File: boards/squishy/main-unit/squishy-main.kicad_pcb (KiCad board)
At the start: 6 copper layers, 0 parts

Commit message: squishy: main: updated the board stackup and went from 6 to 8 layers
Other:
- copper layers 6 -> 8

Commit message: squishy: main: handful of misc updates all jumbled together
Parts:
- added C1: 10n, Capacitor_SMD:C_0603_1608Metric, F.Cu at (203.4, 112.9)
- added C10: 100n, Capacitor_SMD:C_0402_1005Metric, F.Cu at (265.3, 88.3)
- added C11: 100n, Capacitor_SMD:C_0603_1608Metric, F.Cu at (253.8, 91.6)
- added C12: 4u7, Capacitor_SMD:C_0603_1608Metric, F.Cu at (253.8, 94.1)
- added C13: 100n, Capacitor_SMD:C_0603_1608Metric, F.Cu at (253.8, 96.6)
- added C14: 100n, Capacitor_SMD:C_0603_1608Metric, F.Cu at (253.8, 99.2)
- added C15: 10n, Capacitor_SMD:C_0603_1608Metric, F.Cu at (257.8, 86.6)
- added C16: 10u, Capacitor_SMD:C_0603_1608Metric, F.Cu at (257.8, 89.1)
- added C17: 1u, Capacitor_SMD:C_0603_1608Metric, F.Cu at (257.8, 91.6)
- added C18: 10n, Capacitor_SMD:C_0603_1608Metric, F.Cu at (257.8, 94.1)
- added C19: 100n, Capacitor_SMD:C_0603_1608Metric, F.Cu at (203.4, 115.4)
- added C2: 100n, Capacitor_SMD:C_0402_1005Metric, F.Cu at (210.7, 36.6)
- added C20: 1u, Capacitor_SMD:C_0603_1608Metric, F.Cu at (203.4, 117.9)
- added C21: 1u, Capacitor_SMD:C_0603_1608Metric, F.Cu at (203.4, 120.4)
- added C22: 10n, Capacitor_SMD:C_0603_1608Metric, F.Cu at (203.4, 122.9)
- added C23: 100n, Capacitor_SMD:C_0603_1608Metric, F.Cu at (203.4, 21.8)
- added C24: 2u2, Capacitor_SMD:C_0603_1608Metric, F.Cu at (203.4, 24.3)
- added C25: 100n, Capacitor_SMD:C_0603_1608Metric, F.Cu at (203.4, 26.9)
- added C26: 12n, Capacitor_SMD:C_0402_1005Metric, F.Cu at (210.7, 44.5)
- added C27: 10u, Capacitor_SMD:C_0805_2012Metric, F.Cu at (244.6, 19.6)
- added C28: 2u2, Capacitor_SMD:C_1812_4532Metric, F.Cu at (255.3, 67.2)
- added C29: 10u, Capacitor_SMD:C_0805_2012Metric, F.Cu at (244.6, 22.6)
- added C3: 100n, Capacitor_SMD:C_0402_1005Metric, F.Cu at (210.7, 38.6)
- added C30: 1u, Capacitor_SMD:C_0603_1608Metric, F.Cu at (203.4, 29.4)
- added C31: 100n, Capacitor_SMD:C_0402_1005Metric, F.Cu at (210.7, 46.5)
- added C32: 10u, Capacitor_SMD:C_0805_2012Metric, F.Cu at (244.6, 25.6)
- added C33: 10u, Capacitor_SMD:C_0805_2012Metric, F.Cu at (244.6, 28.6)
- added C34: 100n, Capacitor_SMD:C_0402_1005Metric, F.Cu at (210.7, 48.4)
- added C35: 100n, Capacitor_SMD:C_0402_1005Metric, F.Cu at (213.6, 36.6)
- added C36: 100n, Capacitor_SMD:C_0402_1005Metric, F.Cu at (213.6, 38.6)
- added C37: 100n, Capacitor_SMD:C_0402_1005Metric, F.Cu at (213.6, 40.6)
- added C38: 820p, Capacitor_SMD:C_0402_1005Metric, F.Cu at (213.6, 42.5)
- added C39: 1u, Capacitor_SMD:C_0603_1608Metric, F.Cu at (203.4, 31.9)
- added C4: 100n, Capacitor_SMD:C_0402_1005Metric, F.Cu at (210.7, 40.6)
- added C40: 1u, Capacitor_SMD:C_0603_1608Metric, F.Cu at (203.4, 34.4)
- added C41: 100n, Capacitor_SMD:C_0402_1005Metric, F.Cu at (213.6, 44.5)
- added C42: 1u, Capacitor_SMD:C_0603_1608Metric, F.Cu at (207.4, 19.3)
- added C43: 1u, Capacitor_SMD:C_0603_1608Metric, F.Cu at (207.4, 21.8)
- added C44: 100n, Capacitor_SMD:C_0402_1005Metric, F.Cu at (213.6, 46.5)
- added C45: 1u, Capacitor_SMD:C_0603_1608Metric, F.Cu at (207.4, 24.3)
- added C46: 1u, Capacitor_SMD:C_0603_1608Metric, F.Cu at (207.4, 26.9)
- added C47: 1u, Capacitor_SMD:C_0603_1608Metric, F.Cu at (207.4, 29.4)
- added C48: 1u, Capacitor_SMD:C_0603_1608Metric, F.Cu at (207.4, 31.9)
- added C49: 300p, Capacitor_SMD:C_0603_1608Metric, F.Cu at (257.8, 96.6)
- added C5: 100n, Capacitor_SMD:C_0402_1005Metric, F.Cu at (210.7, 42.5)
- added C50: 100n, Capacitor_SMD:C_0402_1005Metric, F.Cu at (213.6, 48.4)
- added C51: 10n, Capacitor_SMD:C_0402_1005Metric, F.Cu at (216.5, 36.6)
- added C52: 100n, Capacitor_SMD:C_0402_1005Metric, F.Cu at (216.5, 38.6)
- added C53: 100n, Capacitor_SMD:C_0402_1005Metric, F.Cu at (216.5, 40.6)
- added C54: 100n, Capacitor_SMD:C_0402_1005Metric, F.Cu at (216.5, 42.5)
- added C55: 10n, Capacitor_SMD:C_0402_1005Metric, F.Cu at (216.5, 44.5)
- added C56: 1n, Capacitor_SMD:C_0402_1005Metric, F.Cu at (216.5, 46.5)
- added C57: 100n, Capacitor_SMD:C_0402_1005Metric, F.Cu at (216.5, 48.4)
- added C58: 10n, Capacitor_SMD:C_0402_1005Metric, F.Cu at (219.3, 36.6)
- added C59: 1n, Capacitor_SMD:C_0402_1005Metric, F.Cu at (219.3, 38.6)
- added C6: 1u, Capacitor_SMD:C_0603_1608Metric, F.Cu at (203.4, 19.3)
- added C60: 100n, Capacitor_SMD:C_0402_1005Metric, F.Cu at (219.3, 40.6)
- added C61: 10n, Capacitor_SMD:C_0402_1005Metric, F.Cu at (219.3, 42.5)
- added C62: 1n, Capacitor_SMD:C_0402_1005Metric, F.Cu at (219.3, 44.5)
- added C63: 1u, Capacitor_SMD:C_0402_1005Metric, F.Cu at (219.3, 46.5)
- added C64: 4u7, Capacitor_SMD:C_0603_1608Metric, F.Cu at (207.4, 34.4)
- added C65: 100n, Capacitor_SMD:C_0402_1005Metric, F.Cu at (219.3, 48.4)
- added C66: 100n, Capacitor_SMD:C_0402_1005Metric, F.Cu at (222.2, 36.6)
- added C67: 10n, Capacitor_SMD:C_0402_1005Metric, F.Cu at (222.2, 38.6)
- added C68: 10n, Capacitor_SMD:C_0402_1005Metric, F.Cu at (222.2, 40.6)
- added C69: 10n, Capacitor_SMD:C_0402_1005Metric, F.Cu at (222.2, 42.5)
- added C7: 1n, Capacitor_SMD:C_0603_1608Metric, F.Cu at (253.8, 86.6)
- added C70: 10n, Capacitor_SMD:C_0402_1005Metric, F.Cu at (222.2, 44.5)
- added C71: 4u7, Capacitor_SMD:C_0603_1608Metric, F.Cu at (211.4, 19.3)
- added C72: 100n, Capacitor_SMD:C_0402_1005Metric, F.Cu at (222.2, 46.5)
- added C73: 100n, Capacitor_SMD:C_0402_1005Metric, F.Cu at (222.2, 48.4)
- added C74: 100n, Capacitor_SMD:C_0402_1005Metric, F.Cu at (225.1, 36.6)
- added C75: 1u, Capacitor_SMD:C_0402_1005Metric, F.Cu at (225.1, 38.6)
- added C76: 1u, Capacitor_SMD:C_0402_1005Metric, F.Cu at (225.1, 40.6)
- added C77: 1u, Capacitor_SMD:C_0402_1005Metric, F.Cu at (225.1, 42.5)
- added C78: 1u, Capacitor_SMD:C_0402_1005Metric, F.Cu at (225.1, 44.5)
- added C79: 100n, Capacitor_SMD:C_0402_1005Metric, F.Cu at (225.1, 46.5)
- added C8: 100n, Capacitor_SMD:C_0603_1608Metric, F.Cu at (253.8, 89.1)
- added C80: 1u, Capacitor_SMD:C_0603_1608Metric, F.Cu at (203.4, 125.4)
- added C81: 100n, Capacitor_SMD:C_0402_1005Metric, F.Cu at (265.3, 90.3)
- added C82: 10n, Capacitor_SMD:C_0402_1005Metric, F.Cu at (265.3, 92.2)
- added C83: 100n, Capacitor_SMD:C_0402_1005Metric, F.Cu at (265.3, 94.2)
- added C84: 10n, Capacitor_SMD:C_0402_1005Metric, F.Cu at (265.3, 96.2)
- added C85: 1n, Capacitor_SMD:C_0402_1005Metric, F.Cu at (265.3, 98.2)
- added C86: 100n, Capacitor_SMD:C_0402_1005Metric, F.Cu at (225.1, 48.4)
- added C87: 1u, Capacitor_SMD:C_0603_1608Metric, F.Cu at (211.4, 21.8)
- added C88: 1u, Capacitor_SMD:C_0603_1608Metric, F.Cu at (211.4, 24.3)
- added C89: 10u, Capacitor_SMD:C_0603_1608Metric, F.Cu at (211.4, 26.9)
- added C9: 100n, Capacitor_SMD:C_0402_1005Metric, F.Cu at (265.3, 86.3)
- added C90: 22p, Capacitor_SMD:C_0603_1608Metric, F.Cu at (211.4, 29.4)
- added C91: 300p, Capacitor_SMD:C_0603_1608Metric, F.Cu at (257.8, 99.2)
- added C92: 100n, Capacitor_SMD:C_0603_1608Metric, F.Cu at (261.9, 86.6)
- added C93: 10u, Capacitor_SMD:C_0805_2012Metric, F.Cu at (276.1, 95.0)
- added C94: 47u, Capacitor_SMD:C_0805_2012Metric, F.Cu at (244.6, 31.6)
- added C95: 100n, Capacitor_SMD:C_0603_1608Metric, F.Cu at (211.4, 31.9)
- added D1: SS10P6-M3/86A, lethalbit-so:TO-277A-2, F.Cu at (256.1, 22.2)
- added D10: GREEN, LED_SMD:LED_0603_1608Metric_Pad1.05x0.95mm_HandSolder, F.Cu at (255.5, 57.0)
- added D11: GREEN, LED_SMD:LED_0603_1608Metric_Pad1.05x0.95mm_HandSolder, F.Cu at (255.5, 59.6)
- added D12: GREEN, LED_SMD:LED_0603_1608Metric_Pad1.05x0.95mm_HandSolder, F.Cu at (255.5, 62.2)
- added D13: 24.25V @ 120mA, Diode_SMD:D_SOD-323, F.Cu at (238.6, 63.9)
- added D14: TN1205H, Package_TO_SOT_SMD:TO-263-2, F.Cu at (237.2, 41.8)
- added D2: BLUE, LED_SMD:LED_0603_1608Metric_Pad1.05x0.95mm_HandSolder, F.Cu at (219.6, 112.9)
- added D3: PINK, LED_SMD:LED_0603_1608Metric_Pad1.05x0.95mm_HandSolder, F.Cu at (219.6, 115.5)
- added D4: WHITE, LED_SMD:LED_0603_1608Metric_Pad1.05x0.95mm_HandSolder, F.Cu at (219.6, 118.1)
- added D5: PINK, LED_SMD:LED_0603_1608Metric_Pad1.05x0.95mm_HandSolder, F.Cu at (219.6, 120.7)
- added D6: BLUE, LED_SMD:LED_0603_1608Metric_Pad1.05x0.95mm_HandSolder, F.Cu at (219.6, 123.3)
- added D7: WHITE, LED_SMD:LED_0603_1608Metric_Pad1.05x0.95mm_HandSolder, F.Cu at (255.5, 49.3)
- added D8: GREEN, LED_SMD:LED_0603_1608Metric_Pad1.05x0.95mm_HandSolder, F.Cu at (255.5, 51.9)
- added D9: GREEN, LED_SMD:LED_0603_1608Metric_Pad1.05x0.95mm_HandSolder, F.Cu at (255.5, 54.5)
- added F1: 7A, Fuse:Fuse_1206_3216Metric, F.Cu at (233.6, 64.1)
- added F2: 7A, Fuse:Fuse_1206_3216Metric, F.Cu at (275.7, 87.0)
- added FB1: 600 @ 100MHz, Resistor_SMD:R_0805_2012Metric, F.Cu at (220.1, 58.7)
- added FB2: 600 @ 100MHz, Resistor_SMD:R_0805_2012Metric, F.Cu at (220.1, 61.7)
- added FID1: Fiducial, Fiducial:Fiducial_0.75mm_Mask1.5mm, F.Cu at (245.8, 37.2)
- added FID2: Fiducial, Fiducial:Fiducial_0.75mm_Mask1.5mm, F.Cu at (245.8, 40.2)
- added FID3: Fiducial, Fiducial:Fiducial_0.75mm_Mask1.5mm, F.Cu at (245.8, 43.3)
- added FID4: Fiducial, Fiducial:Fiducial_0.75mm_Mask1.5mm, F.Cu at (245.8, 46.3)
- added FID5: Fiducial, Fiducial:Fiducial_0.75mm_Mask1.5mm, F.Cu at (248.8, 37.2)
- added FID6: Fiducial, Fiducial:Fiducial_0.75mm_Mask1.5mm, F.Cu at (248.8, 40.2)
- added G1: Antifaschistische_Aktion, lethalbit-graphics:Antifaschistische Aktion_600dpi, F.Cu at (233.9, 26.6)
- added H1: MountingHole, MountingHole:MountingHole_3.2mm_M3_Pad, F.Cu at (205.3, 39.6)
- added H2: MountingHole, MountingHole:MountingHole_3.2mm_M3_Pad, F.Cu at (205.3, 47.6)
- added H3: MountingHole, MountingHole:MountingHole_3.2mm_M3_Pad, F.Cu at (205.3, 55.5)
- added H4: MountingHole, MountingHole:MountingHole_3.2mm_M3_Pad, F.Cu at (205.3, 63.5)
- added J1: REFCLK, lethalbit-rf:Molex_SMA_732512120, F.Cu at (207.4, 106.4)
- added J2: TRIGGER, lethalbit-rf:Molex_SMA_732512120, F.Cu at (219.5, 106.4)
- added J3: USB_C_Receptacle, rhais_usb:USB-3.1-Type-C_In-PCB, F.Cu at (259.6, 77.4)
- added J4: SU SWD, lethalbit-connectors:FTSH-105-01-L-DV-K-TR, F.Cu at (245.8, 114.6)
- added J5: Jack-DC, rhais_connector-jack:BarrelJack_GCT_DCJ200-10-A_Horizontal, F.Cu at (246.5, 50.0)
- added J6: MEM2061-01-188-00-A, lethalbit-connectors:GCT_MEM2061-01-188-00-A_REVA, F.Cu at (233.6, 119.2)
- added J7: SCSI PHY Mezz, lethalbit-connectors:101445x-10x80xLF, F.Cu at (225.4, 77.7)
- added JP1: PD_ONLY, Jumper:SolderJumper-2_P1.3mm_Open_TrianglePad1.0x1.5mm, F.Cu at (232.9, 67.5)
- added L1: 1u5, lethalbit-inductor:Bourns-SRF1260, F.Cu at (233.8, 55.2)
- added L2: 2u2, Inductor_SMD:L_0603_1608Metric, F.Cu at (211.4, 34.4)
- added LED1: SU_STATUS, rhais_led:LED0606, F.Cu at (246.4, 102.9)
- added Q1: NTMFS5C442NT1G, lethalbit-so:ONSemi_SO-8FL_488AA, F.Cu at (250.9, 31.9)
- added Q10: PFET, lethalbit-so:PowerPAK_SO-8L_Dual, F.Cu at (218.6, 53.3)
- added Q2: NX6008NBKR, Package_TO_SOT_SMD:SOT-23, F.Cu at (211.8, 51.6)
- added Q3: NX6008NBKR, Package_TO_SOT_SMD:SOT-23, F.Cu at (211.8, 56.1)
- added Q4: NX6008NBKR, Package_TO_SOT_SMD:SOT-23, F.Cu at (211.8, 60.5)
- added Q5: NX6008NBKR, Package_TO_SOT_SMD:SOT-23, F.Cu at (211.8, 65.0)
- added Q6: PMPB20EN, lethalbit-so:SOT1220-3, F.Cu at (237.1, 67.5)
- added Q8: DMN65D8L-7, Package_TO_SOT_SMD:SOT-23, F.Cu at (211.8, 69.5)
- added R1: 1k, Resistor_SMD:R_0603_1608Metric, F.Cu at (207.4, 112.9)
- added R10: 8k06, Resistor_SMD:R_0603_1608Metric, F.Cu at (261.9, 94.1)
- added R11: 100, Resistor_SMD:R_0603_1608Metric, F.Cu at (261.9, 96.6)
- added R12: 10k, Resistor_SMD:R_0603_1608Metric, F.Cu at (207.4, 120.4)
- added R13: 100, Resistor_SMD:R_0603_1608Metric, F.Cu at (207.4, 122.9)
- added R14: 10K, rhais_rcl:R0603_Array_Concave_4, F.Cu at (247.3, 121.0)
- added R15: 5k36, Resistor_SMD:R_0603_1608Metric, F.Cu at (215.4, 21.8)
- added R16: 10m, Resistor_SMD:R_0603_1608Metric, F.Cu at (215.4, 24.3)
- added R17: 10k, Resistor_SMD:R_0603_1608Metric, F.Cu at (215.4, 26.9)
- added R18: 40k, Resistor_SMD:R_0603_1608Metric, F.Cu at (215.4, 29.4)
- added R19: 1k, Resistor_SMD:R_0603_1608Metric, F.Cu at (207.4, 125.4)
- added R2: 70k, Resistor_SMD:R_0402_1005Metric, F.Cu at (228.0, 67.9)
- added R20: 1k, Resistor_SMD:R_0603_1608Metric, F.Cu at (211.4, 112.9)
- added R21: 1k, Resistor_SMD:R_0603_1608Metric, F.Cu at (211.4, 115.4)
- added R22: 1k, Resistor_SMD:R_0603_1608Metric, F.Cu at (211.4, 117.9)
- added R23: 4k7, Resistor_SMD:R_0603_1608Metric, F.Cu at (211.4, 120.4)
- added R24: 10k, Resistor_SMD:R_0603_1608Metric, F.Cu at (211.4, 122.9)
- added R25: 6k8, Resistor_SMD:R_0603_1608Metric, F.Cu at (211.4, 125.4)
- added R26: 10k, Resistor_SMD:R_0603_1608Metric, F.Cu at (215.4, 112.9)
- added R27: 4k7, Resistor_SMD:R_0603_1608Metric, F.Cu at (215.4, 115.4)
- added R28: 10k, Resistor_SMD:R_0603_1608Metric, F.Cu at (215.4, 117.9)
- added R29: 0, Resistor_SMD:R_0402_1005Metric, F.Cu at (245.6, 105.6)
- added R3: 35k, Resistor_SMD:R_0402_1005Metric, F.Cu at (228.0, 69.9)
- added R30: 0, Resistor_SMD:R_0402_1005Metric, F.Cu at (268.2, 98.6)
- added R31: 6k8, Resistor_SMD:R_0603_1608Metric, F.Cu at (215.4, 31.9)
- added R32: 10k, Resistor_SMD:R_0603_1608Metric, F.Cu at (215.4, 34.4)
- added R33: 300k, Resistor_SMD:R_0603_1608Metric, F.Cu at (219.4, 19.3)
- added R34: 10k, Resistor_SMD:R_0603_1608Metric, F.Cu at (219.4, 21.8)
- added R35: 10k, Resistor_SMD:R_0603_1608Metric, F.Cu at (219.4, 24.3)
- added R36: 10k, Resistor_SMD:R_0603_1608Metric, F.Cu at (219.4, 26.9)
- added R37: 10k, Resistor_SMD:R_0603_1608Metric, F.Cu at (219.4, 29.4)
- added R38: 10k, Resistor_SMD:R_0603_1608Metric, F.Cu at (219.4, 31.9)
- added R39: 10k, Resistor_SMD:R_0603_1608Metric, F.Cu at (219.4, 34.4)
- added R4: 10k, Resistor_SMD:R_0603_1608Metric, F.Cu at (215.4, 19.3)
- added R40: 10k, Resistor_SMD:R_0603_1608Metric, F.Cu at (223.4, 19.3)
- added R41: 1M, Resistor_SMD:R_0603_1608Metric, F.Cu at (215.4, 120.4)
- added R42: 4k7, Resistor_SMD:R_0603_1608Metric, F.Cu at (223.4, 21.8)
- added R43: 150k, Resistor_SMD:R_0603_1608Metric, F.Cu at (223.4, 24.3)
- added R44: 10k, Resistor_SMD:R_0603_1608Metric, F.Cu at (223.4, 26.9)
- added R45: 10k, Resistor_SMD:R_0603_1608Metric, F.Cu at (223.4, 29.4)
- added R46: 10K, rhais_rcl:R0603_Array_Concave_4, F.Cu at (242.8, 67.0)
- added R47: 52, Resistor_SMD:R_0603_1608Metric, F.Cu at (223.4, 31.9)
- added R48: 10K, rhais_rcl:R0603_Array_Concave_4, F.Cu at (246.4, 67.0)
- added R49: 4k7, rhais_rcl:R0603_Array_Concave_4, F.Cu at (275.4, 75.9)
- added R5: 4k7, Resistor_SMD:R_0603_1608Metric, F.Cu at (207.4, 115.4)
- added R50: 10K, rhais_rcl:R0603_Array_Concave_4, F.Cu at (250.0, 67.0)
- added R6: 4k7, rhais_rcl:R0603_Array_Concave_4, F.Cu at (243.7, 121.0)
- added R7: 1k, Resistor_SMD:R_0603_1608Metric, F.Cu at (207.4, 117.9)
- added R8: 1M, Resistor_SMD:R_0603_1608Metric, F.Cu at (261.9, 89.1)
- added R9: 10k, Resistor_SMD:R_0603_1608Metric, F.Cu at (261.9, 91.6)
- added SW1: RST, lethalbit:SW_Tactile_SPST_Angled_TC-1109DE, F.Cu at (249.9, 26.7)
- added TP1: 5V, TestPoint:TestPoint_Pad_D1.0mm, F.Cu at (248.8, 43.3)
- added TP10: VCC, TestPoint:TestPoint_Pad_D1.0mm, F.Cu at (254.9, 46.3)
- added TP11: 1v2, TestPoint:TestPoint_Pad_D1.0mm, F.Cu at (257.9, 37.2)
- added TP12: GND, TestPoint:TestPoint_Pad_D1.0mm, F.Cu at (257.9, 40.2)
- added TP13: 1v8, TestPoint:TestPoint_Pad_D1.0mm, F.Cu at (257.9, 43.3)
- added TP14: VBUS, TestPoint:TestPoint_Pad_D1.0mm, F.Cu at (257.9, 46.3)
- added TP2: 1v2A, TestPoint:TestPoint_Pad_D1.0mm, F.Cu at (248.8, 46.3)
- added TP3: GND, TestPoint:TestPoint_Pad_D1.0mm, F.Cu at (251.8, 37.2)
- added TP4: 2v5, TestPoint:TestPoint_Pad_D1.0mm, F.Cu at (251.8, 40.2)
- added TP5: GND, TestPoint:TestPoint_Pad_D1.0mm, F.Cu at (251.8, 43.3)
- added TP6: 3v3, TestPoint:TestPoint_Pad_D1.0mm, F.Cu at (251.8, 46.3)
- added TP7: GND, TestPoint:TestPoint_Pad_D1.0mm, F.Cu at (254.9, 37.2)
- added TP8: VDC, TestPoint:TestPoint_Pad_D1.0mm, F.Cu at (254.9, 40.2)
- added TP9: GND, TestPoint:TestPoint_Pad_D1.0mm, F.Cu at (254.9, 43.3)
- added U1: LFE5UM5G-45F-8BG381C, lethalbit:318caBGA, F.Cu at (234.9, 101.1)
- added U10: FUSB302BMPX, Package_DFN_QFN:WQFN-14-1EP_2.5x2.5mm_P0.5mm_EP1.45x1.45mm, F.Cu at (275.4, 82.3)
- added U11: ATSAMD09D14A-M, Package_DFN_QFN:QFN-24-1EP_4x4mm_P0.5mm_EP2.6x2.6mm, F.Cu at (245.8, 84.8)
- added U12: GD25Q64EWIGR, rhais_package-qfn:UDFN-8-1EP_6x5mm_P1.27mm_EP3.4x4mm, F.Cu at (238.3, 85.2)
- added U13: LM51551DSSR, lethalbit:WSON-12-1EP_2x3mm_P0.5mm_EP1x2.65mm, F.Cu at (257.1, 30.7)
- added U14: HyperRAM, lethalbit-memory:TFBGA-24-6x8mm-1.0mm, F.Cu at (221.7, 86.8)
- added U15: HyperRAM, lethalbit-memory:TFBGA-24-6x8mm-1.0mm, F.Cu at (229.8, 86.8)
- added U16: TPS7A1112PDRVT, Package_SON:WSON-6-1EP_2x2mm_P0.65mm_EP1x1.6mm, F.Cu at (216.0, 59.0)
- added U17: TPS7A1125PDRVT, Package_SON:WSON-6-1EP_2x2mm_P0.65mm_EP1x1.6mm, F.Cu at (216.0, 62.6)
- added U18: TPS73733DRVR, Package_SON:WSON-6-1EP_2x2mm_P0.65mm_EP1x1.6mm, F.Cu at (216.0, 66.1)
- added U2: HyperRAM, lethalbit-memory:TFBGA-24-6x8mm-1.0mm, F.Cu at (205.4, 86.8)
- added U20: TPS7A1112PDRVT, Package_SON:WSON-6-1EP_2x2mm_P0.65mm_EP1x1.6mm, F.Cu at (216.0, 69.7)
- added U21: AP3428/A, Package_TO_SOT_SMD:TSOT-23-6, F.Cu at (220.5, 65.4)
- added U3: HyperRAM, lethalbit-memory:TFBGA-24-6x8mm-1.0mm, F.Cu at (213.5, 86.8)
- added U4: APX811-40UG-7, Package_TO_SOT_SMD:SOT-143, F.Cu at (228.7, 64.7)
- added U5: HD3SS460, rhais_package-qfn:WQFN-28-1EP_3.5x5.5_P0.5mm_EP2x4mm, F.Cu at (269.8, 89.4)
- added U6: TPD4E02B04DQA, rhais_package-qfn:USON-10_2.5x1.0mm_P0.5mm, F.Cu at (268.5, 95.6)
- added U7: SP3400-02UTG, rhais_package-qfn:UDFN-6L, F.Cu at (275.6, 98.1)
- added U8: TPD4E02B04DQA, rhais_package-qfn:USON-10_2.5x1.0mm_P0.5mm, F.Cu at (272.1, 95.6)
- added U9: USB3318, Package_DFN_QFN:QFN-24-1EP_4x4mm_P0.5mm_EP2.6x2.6mm, F.Cu at (270.4, 76.8)
- added X1: 100MHz, lethalbit:AK3A-xxxMHz, F.Cu at (246.7, 99.1)
- added X2: 13MHz, rhais_osc:SMD3225, F.Cu at (270.2, 82.5)
- added X3: 200MHz, lethalbit:AK3A-xxxMHz, F.Cu at (275.4, 90.8)
- added X4: 48MHz, rhais_osc:SMD3225, F.Cu at (247.0, 94.4)
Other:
- board outline added: 10 x 5.2 mm
- rule pad_to_mask_clearance: 0.038 -> 0.05
- board text added: "Impedance Table: 90Ω Coplanar Differential (inner): trace/space: (0.1717/0.1800) clearance: 0.2500mm 90Ω Coplanar Differential (outter): trace/space: (0.1699/0.1800) clearance: 0.2500mm"

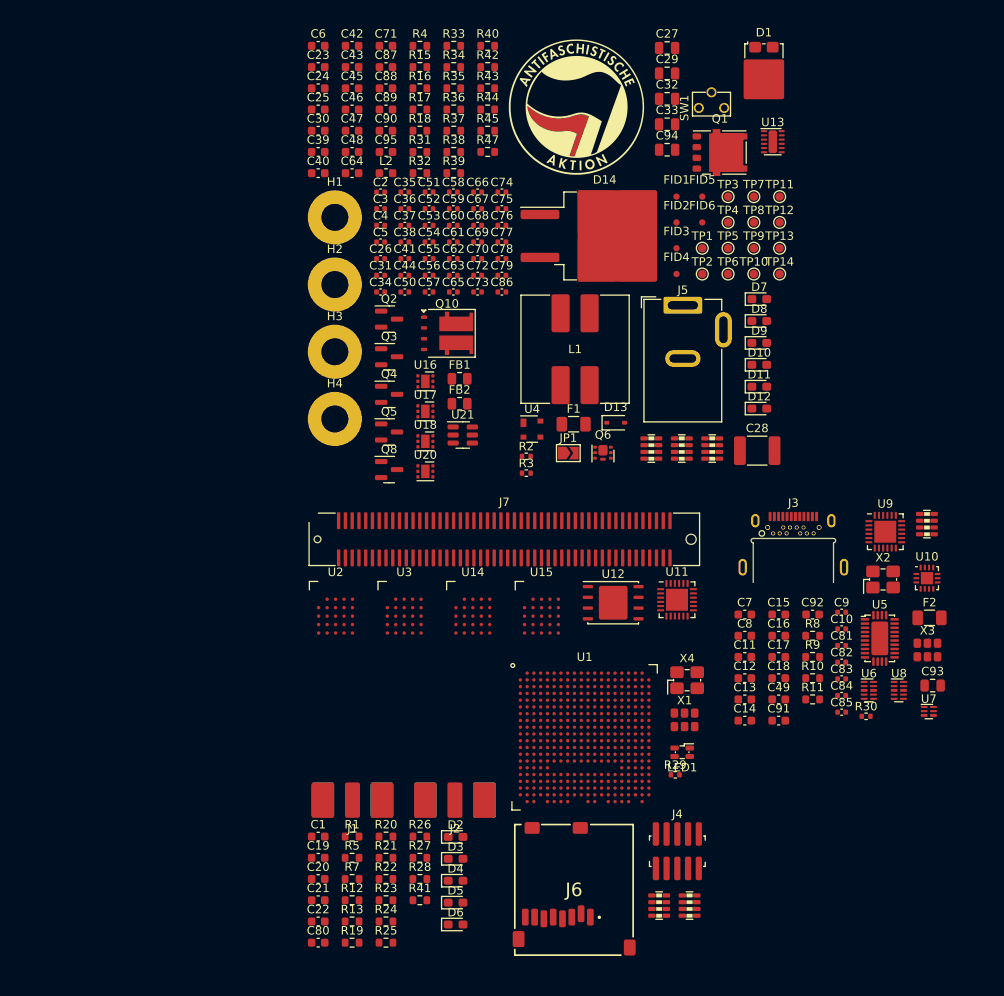
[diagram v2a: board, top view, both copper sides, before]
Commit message: squishy: main: Added a whole bunch of test points
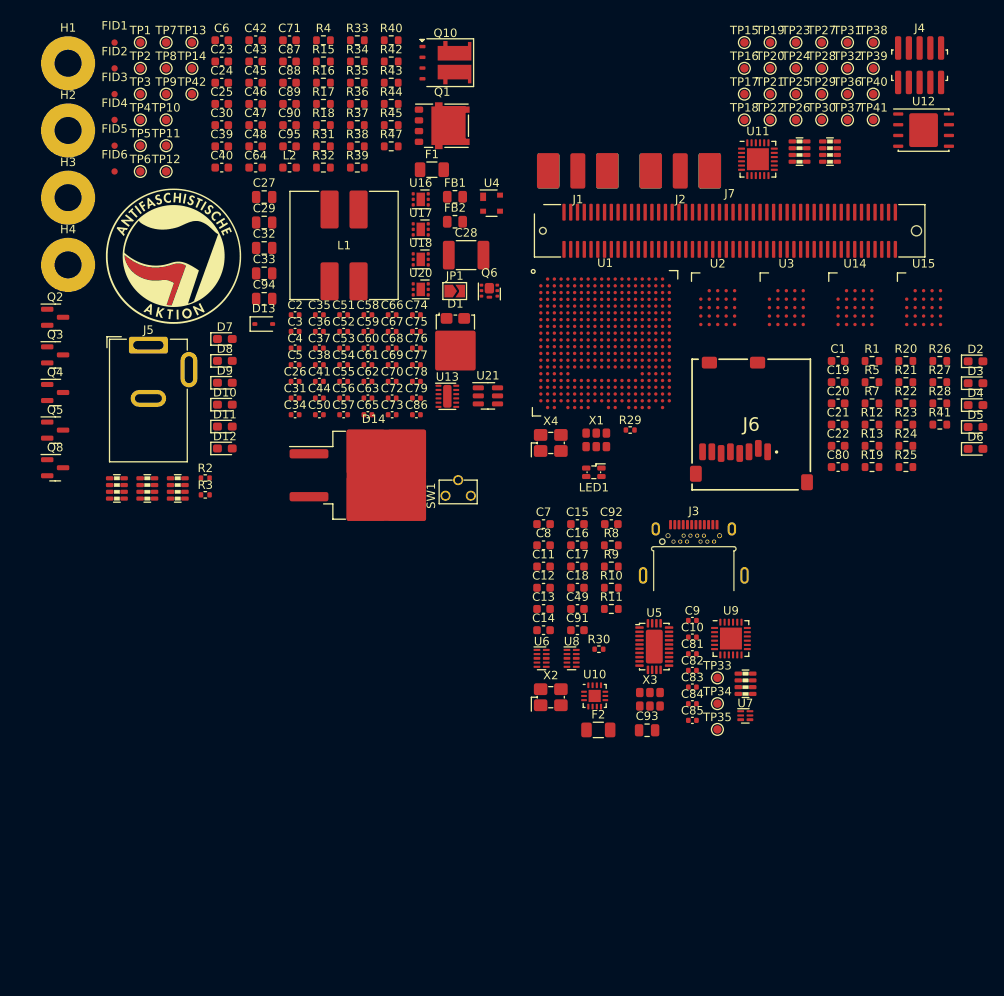
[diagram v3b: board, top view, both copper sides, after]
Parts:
- added TP15: FPGA_TDO, TestPoint:TestPoint_Pad_D1.0mm, F.Cu at (253.8, 18.9)
- added TP16: FPGA_TCK, TestPoint:TestPoint_Pad_D1.0mm, F.Cu at (253.8, 22.0)
- added TP17: FPGA_TDI, TestPoint:TestPoint_Pad_D1.0mm, F.Cu at (253.8, 25.0)
- added TP18: FPGA_TMS, TestPoint:TestPoint_Pad_D1.0mm, F.Cu at (253.8, 28.1)
- added TP19: FPGA_TMS, TestPoint:TestPoint_Pad_D1.0mm, F.Cu at (256.8, 18.9)
- added TP20: SU_ATTN, TestPoint:TestPoint_Pad_D1.0mm, F.Cu at (256.8, 22.0)
- added TP21: FPGA_COPI, TestPoint:TestPoint_Pad_D1.0mm, F.Cu at (256.8, 25.0)
- added TP22: FPGA_CIPO, TestPoint:TestPoint_Pad_D1.0mm, F.Cu at (256.8, 28.1)
- added TP23: ~{FPGA_INIT}, TestPoint:TestPoint_Pad_D1.0mm, F.Cu at (259.9, 18.9)
- added TP24: ~{FPGA_PROG}, TestPoint:TestPoint_Pad_D1.0mm, F.Cu at (259.9, 22.0)
- added TP25: FPGA_CCLK, TestPoint:TestPoint_Pad_D1.0mm, F.Cu at (259.9, 25.0)
- added TP26: ~{FPGA_CS}, TestPoint:TestPoint_Pad_D1.0mm, F.Cu at (259.9, 28.1)
- added TP27: FLASH_CIPO, TestPoint:TestPoint_Pad_D1.0mm, F.Cu at (262.9, 18.9)
- added TP28: FLASH_COPI, TestPoint:TestPoint_Pad_D1.0mm, F.Cu at (262.9, 22.0)
- added TP29: FLASH_CLK, TestPoint:TestPoint_Pad_D1.0mm, F.Cu at (262.9, 25.0)
- added TP30: ~{FLASH_CS}, TestPoint:TestPoint_Pad_D1.0mm, F.Cu at (262.9, 28.1)
- added TP31: SU_SWDIO, TestPoint:TestPoint_Pad_D1.0mm, F.Cu at (266.0, 18.9)
- added TP32: SU_SWCLK, TestPoint:TestPoint_Pad_D1.0mm, F.Cu at (266.0, 22.0)
- added TP33: ~{PD_INIT}, TestPoint:TestPoint_Pad_D1.0mm, F.Cu at (250.6, 94.1)
- added TP34: PD_SCA, TestPoint:TestPoint_Pad_D1.0mm, F.Cu at (250.6, 97.1)
- added TP35: PD_SCL, TestPoint:TestPoint_Pad_D1.0mm, F.Cu at (250.6, 100.2)
- added TP36: RAM ~{CS0}, TestPoint:TestPoint_Pad_D1.0mm, F.Cu at (266.0, 25.0)
- added TP37: RAM ~{CS1}, TestPoint:TestPoint_Pad_D1.0mm, F.Cu at (266.0, 28.1)
- added TP38: RAM ~{CS2}, TestPoint:TestPoint_Pad_D1.0mm, F.Cu at (269.0, 18.9)
- added TP39: RAM ~{CS3}, TestPoint:TestPoint_Pad_D1.0mm, F.Cu at (269.0, 22.0)
- added TP40: RAM ~{RST}, TestPoint:TestPoint_Pad_D1.0mm, F.Cu at (269.0, 25.0)
- added TP41: RAM RWDS, TestPoint:TestPoint_Pad_D1.0mm, F.Cu at (269.0, 28.1)
- added TP42: PSU_EN, TestPoint:TestPoint_Pad_D1.0mm, F.Cu at (188.4, 25.0)
- moved J4 97.3 mm to (274.5, 21.6)
- moved R14 90.7 mm to (263.9, 31.8)
- moved R6 90.7 mm to (260.3, 31.8)
- moved C1 83.4 mm to (264.9, 56.6)
- moved C20 83.4 mm to (264.9, 61.6)
- moved C21 83.4 mm to (264.9, 64.1)
- moved D3 83.4 mm to (281.1, 59.2)
- moved D4 83.4 mm to (281.1, 61.8)
- moved D5 83.4 mm to (281.1, 64.4)
- moved R1 83.4 mm to (268.9, 56.6)
- moved R12 83.4 mm to (268.9, 64.1)
- moved R20 83.4 mm to (272.9, 56.6)
- moved R22 83.4 mm to (272.9, 61.6)
- moved R23 83.4 mm to (272.9, 64.1)
- moved R26 83.4 mm to (276.9, 56.6)
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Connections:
- U1 pad P4: /SYSCLK+ -> /SYSCLK-

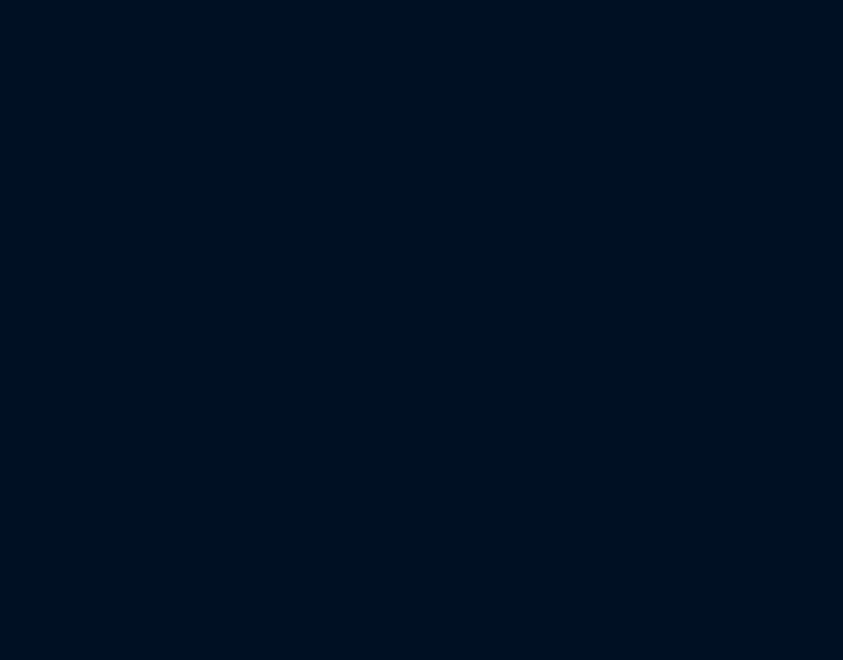
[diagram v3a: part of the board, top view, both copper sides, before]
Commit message: squishy: main: re-synced the PCB and schematic, no layout yet, schematic still needs some work
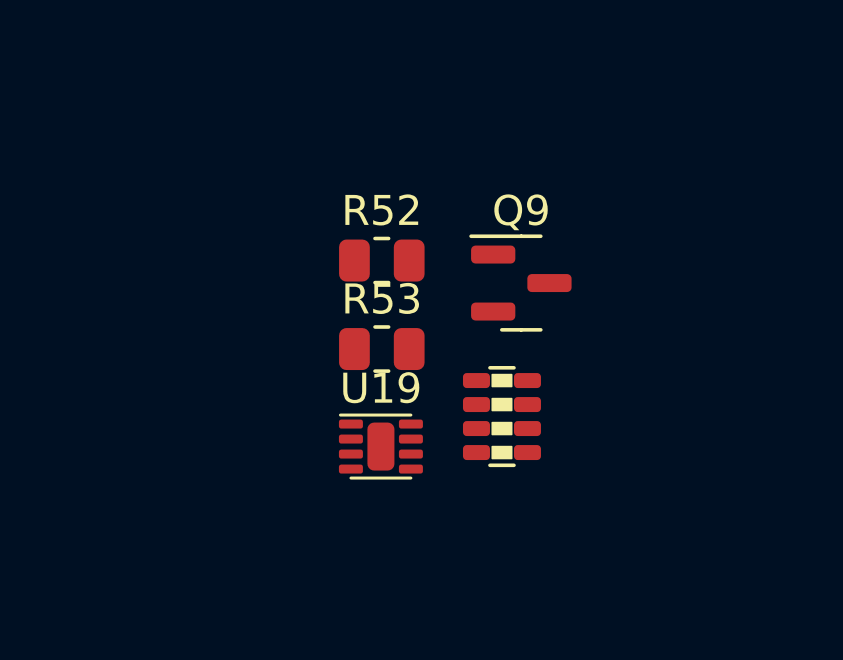
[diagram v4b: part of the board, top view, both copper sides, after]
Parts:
- added Q9: DMN65D8L-7, Package_TO_SOT_SMD:SOT-23, F.Cu at (273.8, 83.3)
- added R51: 10K, rhais_rcl:R0603_Array_Concave_4, F.Cu at (273.1, 87.8)
- added R52: 100m, Resistor_SMD:R_0805_2012Metric, F.Cu at (269.1, 82.6)
- added R53: 100m, Resistor_SMD:R_0805_2012Metric, F.Cu at (269.1, 85.5)
- added U19: INAx180, lethalbit:WSON_8_2x2mm_1EP, F.Cu at (269.1, 88.8)
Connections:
- J7 pad 1: +3V3 -> Net-(J7-Pin_1)
- J7 pad 2: +5V -> Net-(J7-Pin_2)
- J7 pad 3: +3V3 -> Net-(J7-Pin_1)
- J7 pad 4: +5V -> Net-(J7-Pin_2)
- J7 pad 5: +3V3 -> Net-(J7-Pin_1)
- J7 pad 6: +5V -> Net-(J7-Pin_2)
- J7 pad 7: +3V3 -> Net-(J7-Pin_1)
- J7 pad 8: +5V -> Net-(J7-Pin_2)
